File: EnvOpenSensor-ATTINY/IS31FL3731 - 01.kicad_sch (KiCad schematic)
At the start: 80 parts, among them IC1 IS31FL3730-QFLS2-TR

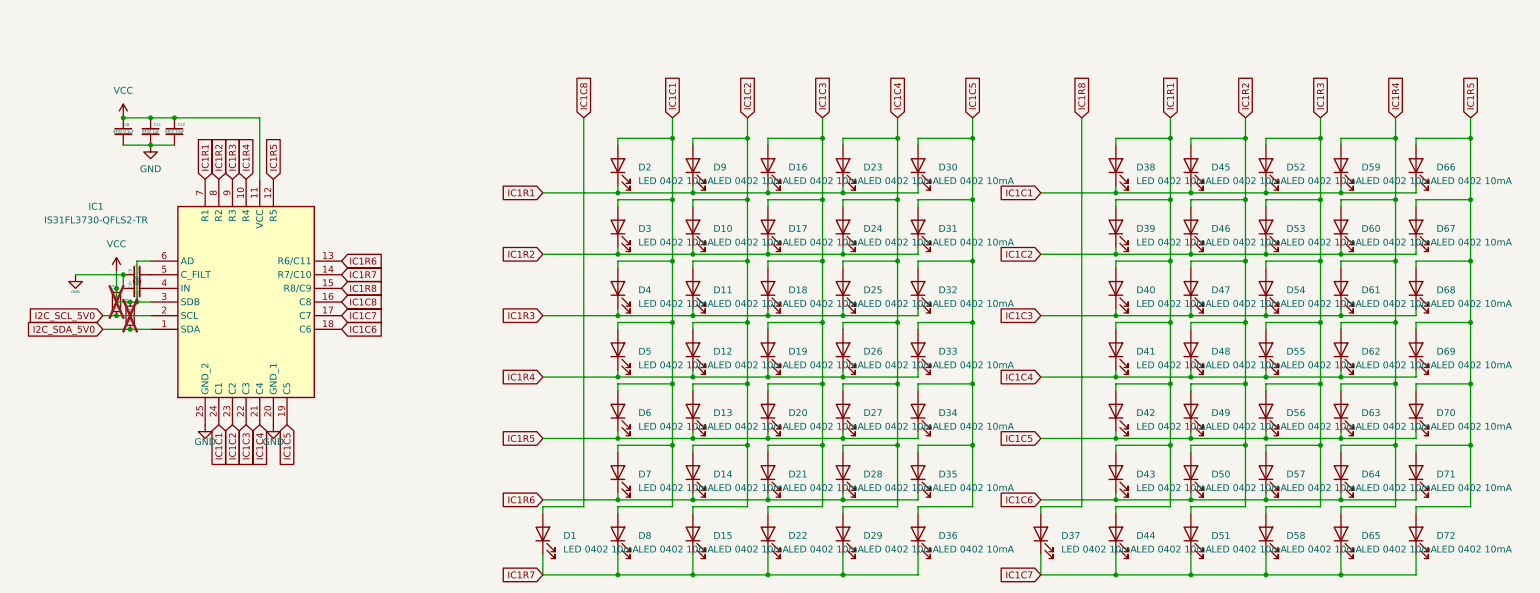
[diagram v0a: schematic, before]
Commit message: added pullup to reset (schematic only)
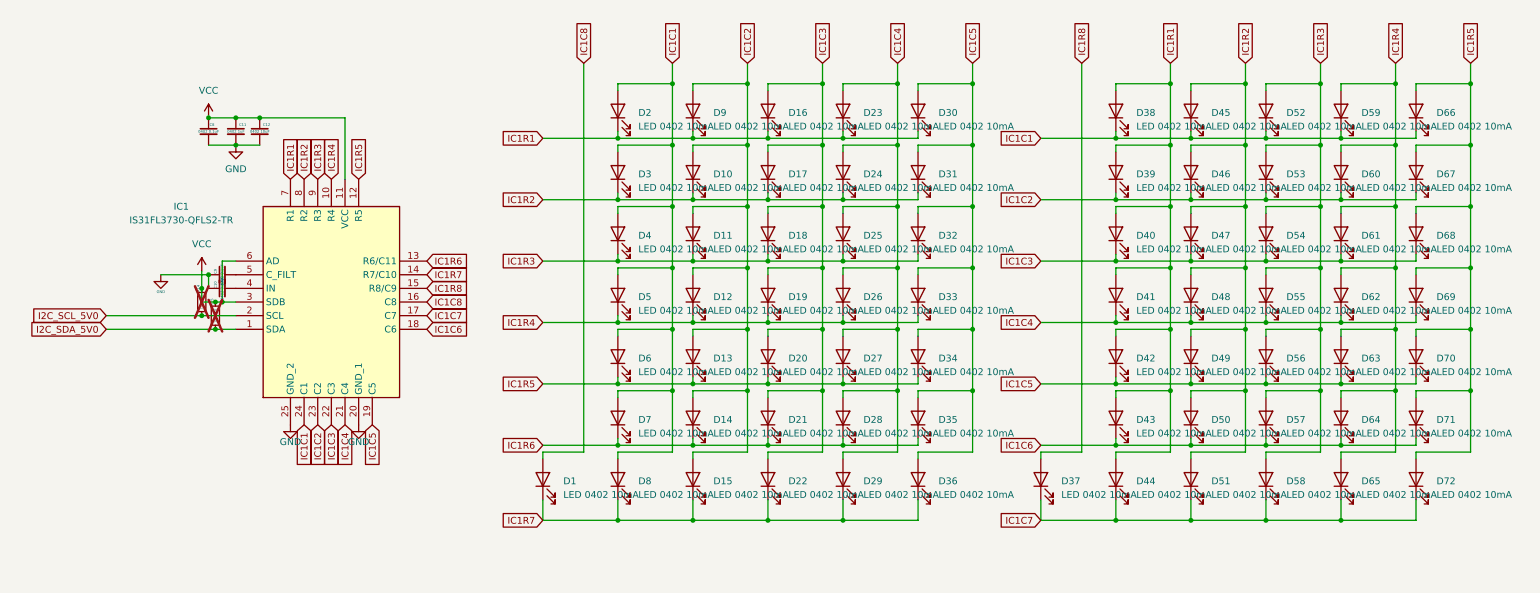
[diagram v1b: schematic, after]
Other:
- moved on the sheet: C10, C11, C12, C8, C9, D1, D10, D11, D12, D13, D14, D15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
